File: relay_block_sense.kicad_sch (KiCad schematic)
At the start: 49 parts, among them J7 Screw_Terminal_01x02, J8 Screw_Terminal_01x10, J9 Screw_Terminal_01x10, U26 TLP3558A, U27 TLP3558A, U28 TLP3558A, U29 TLP3558A, U30 TLP3558A, U31 TLP3558A, U32 TLP3558A, U33 TLP3558A, U34 TLP3558A, U35 TLP3558A, U36 TLP3558A, U37 TLP3558A, U38 TLP3558A, U39 TLP3558A, U40 TLP3558A, U41 TLP3558A, U42 TLP3558A, U43 TLP3558A, U44 TLP3558A, U45 TLP3558A, U46 TLP3558A, U47 TLP3558A

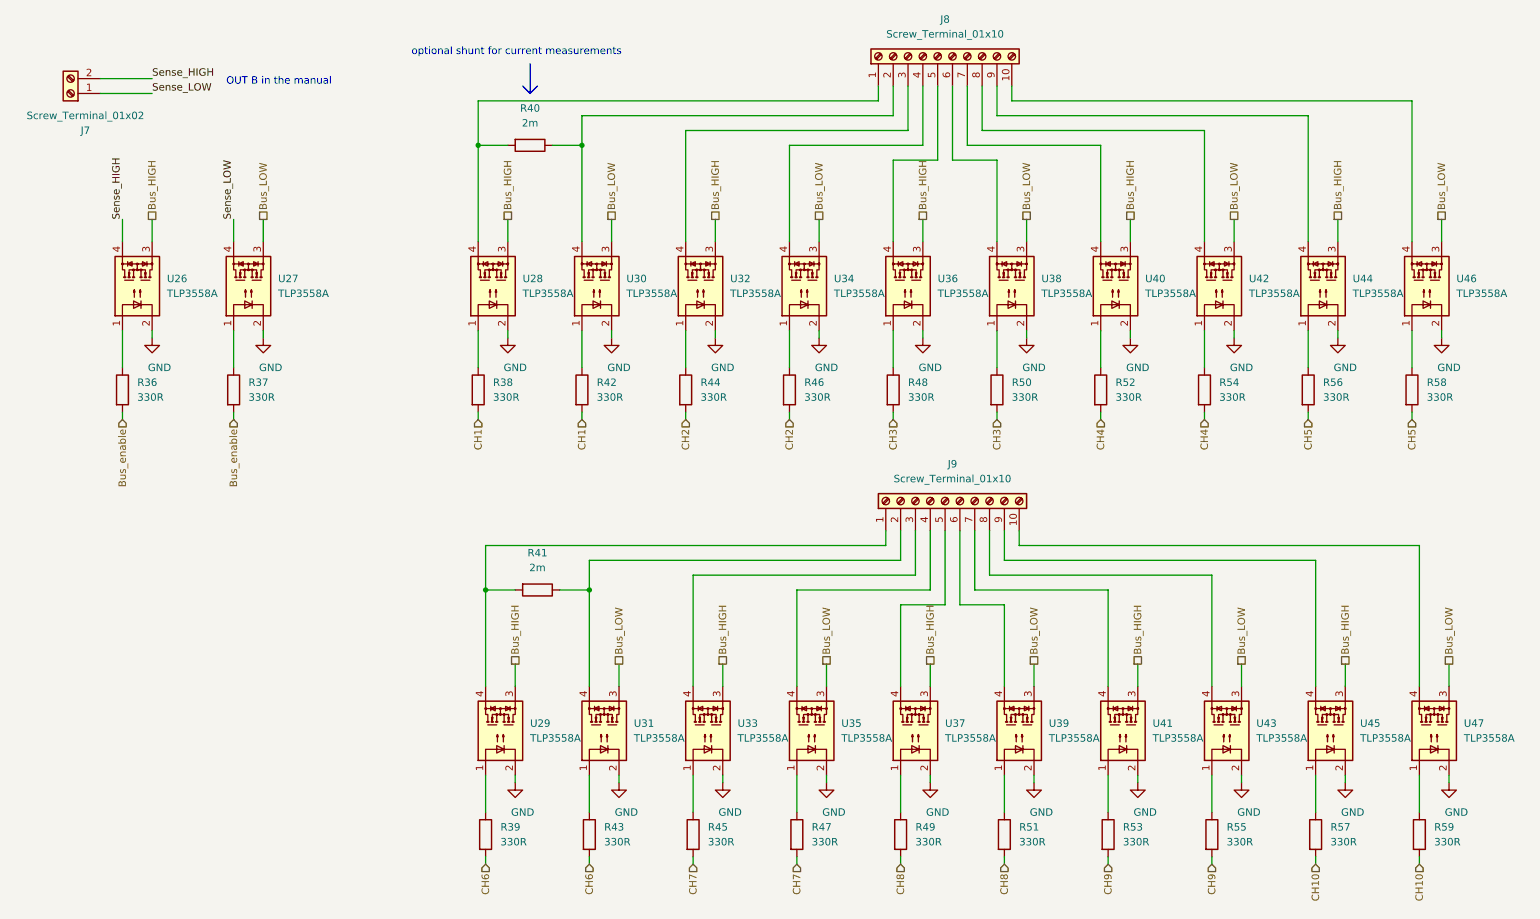
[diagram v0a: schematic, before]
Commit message: Version 1.6
Created a high-voltage rated scan board.

Control is done completely in logic to avoid programming an MCU
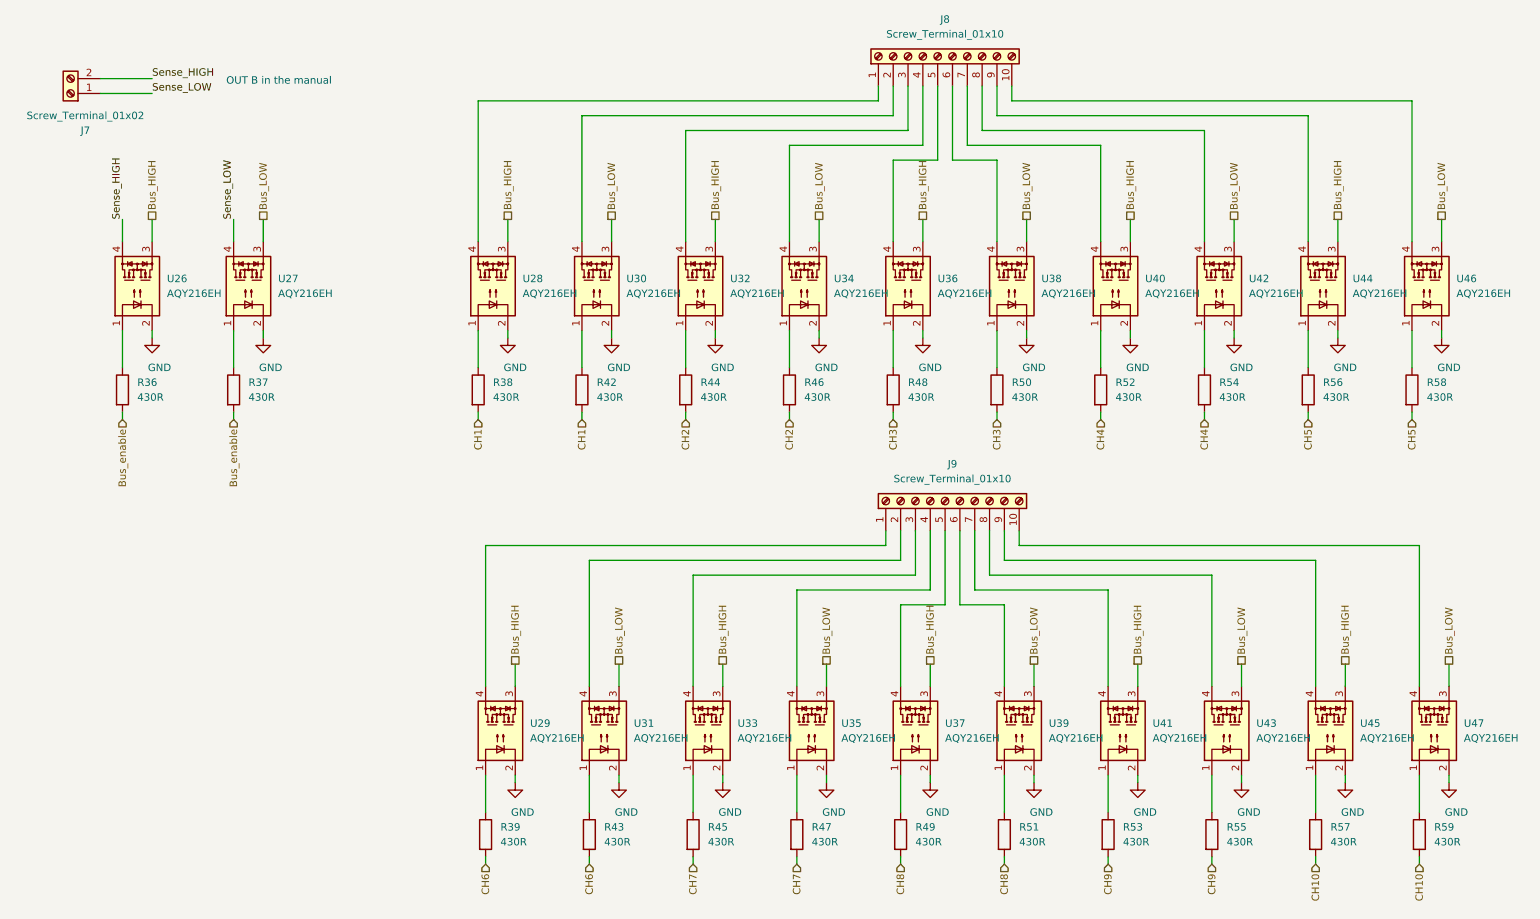
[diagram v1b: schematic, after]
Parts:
- removed R40, R41: 2m, Resistor_SMD:R_2512_6332Metric, symbol Device:R
- R36, R37, R38, R39, R42, R43, R44, R45, R46, R47, R48, R49, R50, R51, R52, R53, R54, R55, R56, R57, R58, R59: value 330R -> 430R
- U26, U27, U28, U29, U30, U31, U32, U33, U34, U35, U36, U37, U38, U39, U40, U41, U42, U43, U44, U45, U46, U47: value TLP3558A -> AQY216EH; footprint Package_DIP:DIP-4_W7.62mm -> Package_DIP:DIP-4_W7.62mm_Least
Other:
- note removed: "optional shunt for current measurements"
